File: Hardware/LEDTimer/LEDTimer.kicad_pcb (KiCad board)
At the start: 2 copper layers, 38 x 27.3 mm, 35 parts, among them J2 LED, J3 PWR_IN, SW1 SW_Push, SW2 SW_Push, SW3 SW_Push, SW4 SW_SPDT, U1 AP7383-36WW7, U2 PIC16F1825, U3 Display_128x64_096_I2C, U4 BCR_421U_E6327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

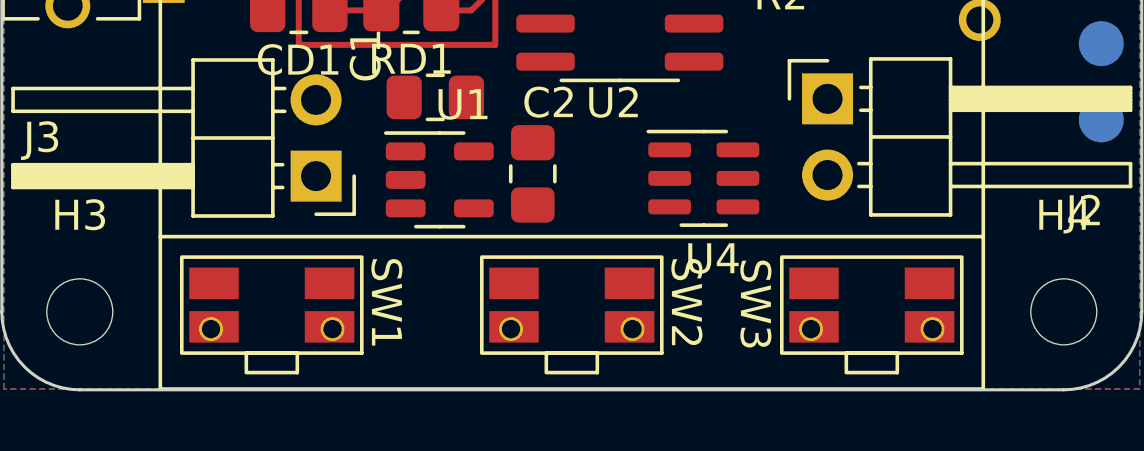
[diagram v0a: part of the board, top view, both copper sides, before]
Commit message: PCB: move the switches closer to the edge
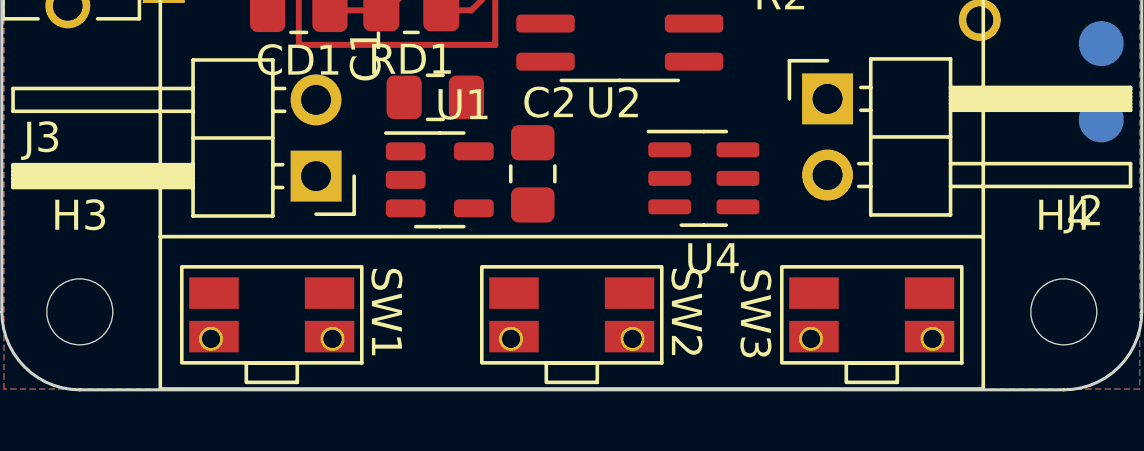
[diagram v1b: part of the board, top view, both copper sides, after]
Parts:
- moved SW1 0.33 mm to (130.3, 104.3)
- moved SW2 0.33 mm to (140.3, 104.3)
- moved SW3 0.33 mm to (150.3, 104.3)
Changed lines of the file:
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@@
   )
   (footprint "LEDTimer:EVQ9P701P" (layer "F.Cu")
-    (at 150.3 103.975 180)
+    (at 150.3 104.3 180)
     (property "Sheetfile" "LEDTimer.kicad_sch")
     (property "Sheetname" "")
@@
   )
   (footprint "LEDTimer:EVQ9P701P" (layer "F.Cu")
-    (at 140.3 103.975 180)
+    (at 140.3 104.3 180)
     (property "Sheetfile" "LEDTimer.kicad_sch")
     (property "Sheetname" "")
@@
   )
   (footprint "LEDTimer:EVQ9P701P" (layer "F.Cu")
-    (at 130.3 103.975 180)
-    (property "Sheetfile" "LEDTimer.kicad_sch")
-    (property "Sheetname" "")
+    (at 130.3 104.3 180)
+    (property "Sheetfile" "LEDTimer.kicad_sch")
+    (property "Sheetname" "")

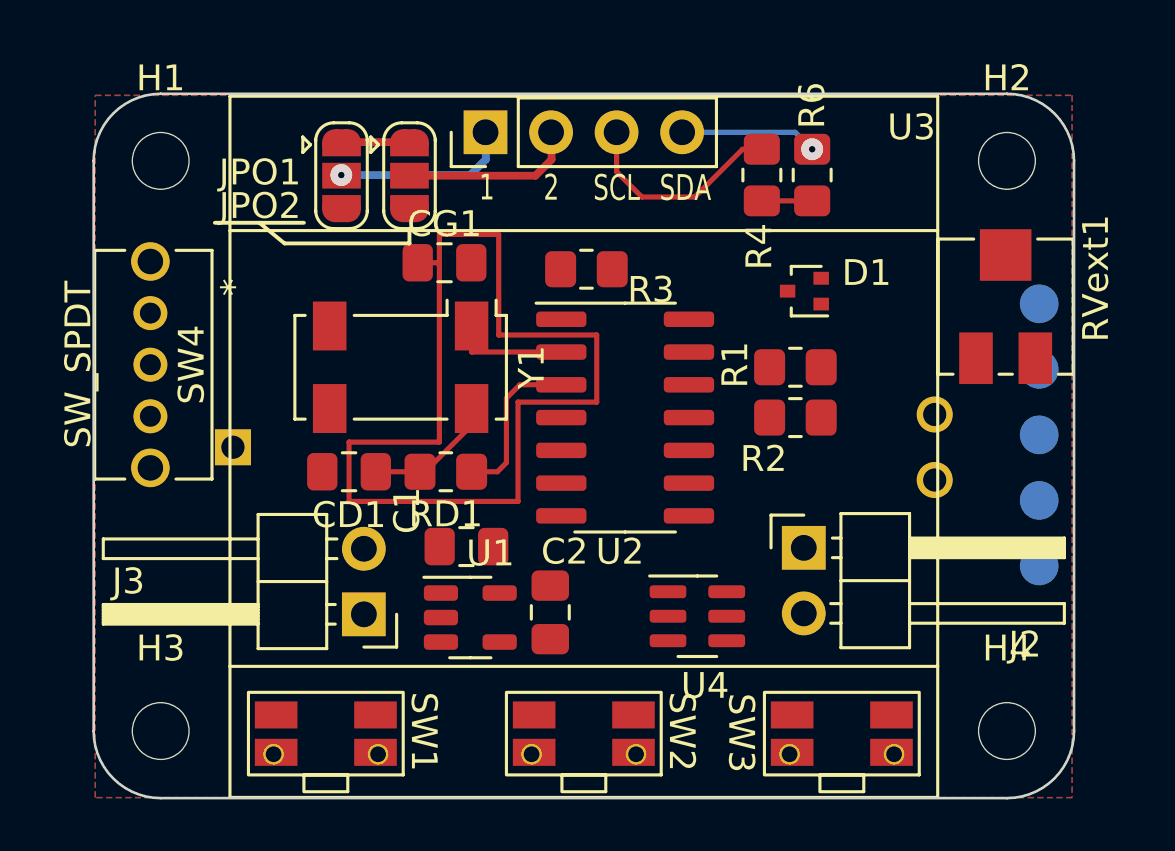
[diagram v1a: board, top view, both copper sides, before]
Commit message: PCB: use a 4-layer design
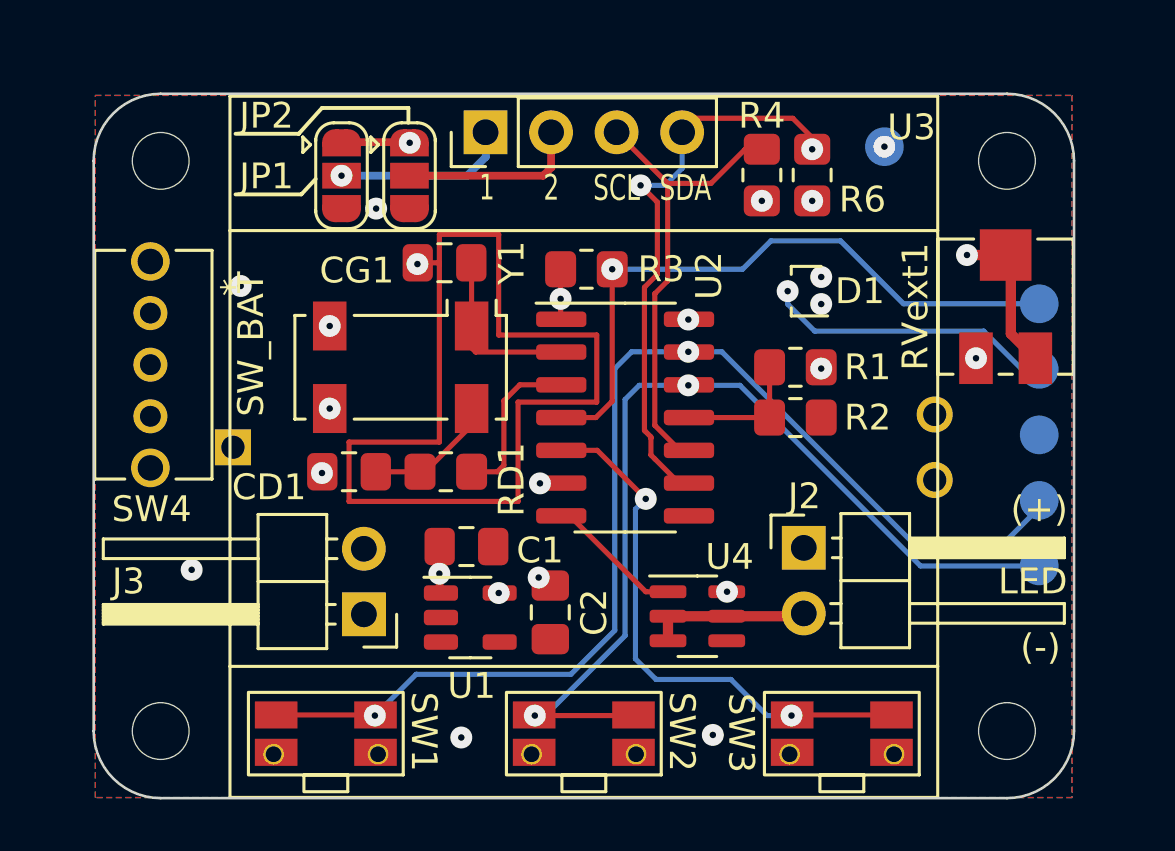
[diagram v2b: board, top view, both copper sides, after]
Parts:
- added TP6: UART_TX, TestPoint:TestPoint_Pad_D1.5mm, B.Cu at (151.9, 81.5)
- SW4: value SW_SPDT -> SW_BAT
- renumbered JPO1 to JP1, JPO2 to JP2
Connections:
- SW4 pad 1: Net-(BT1-Pad2) -> unconnected-(SW4-Pad1)
- SW4 pad 3: unconnected-(SW4-Pad3) -> Net-(BT1-Pad2)
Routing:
- net Net-(D1-Pad2): track 0.00 -> 48.6 mm, vias 0 -> 1
- net Net-(BT1-Pad2): track 0.00 -> 47.9 mm
- net /ICSPDAT: track 0.00 -> 45.7 mm, vias 0 -> 2
- net /ICSPCLK: track 0.00 -> 36.9 mm, vias 0 -> 2
- net +3V3: track 4.59 -> 40.7 mm, vias 0 -> 5
- net Net-(RVext1-Pad1): track 0.00 -> 31.0 mm, vias 0 -> 2
- net /~{MCLR}/VPP: track 0.00 -> 25.4 mm, vias 0 -> 1
- net /UART_TX: track 0.00 -> 23.3 mm, vias 0 -> 2
- net +5V: track 0.00 -> 21.5 mm, vias 0 -> 1
- net Net-(SW3-Pad2): track 0.00 -> 21.2 mm, vias 0 -> 2
- net Net-(C2-Pad1): track 0.00 -> 19.4 mm, vias 0 -> 4
- net Net-(R6-Pad2): track 5.31 -> 22.3 mm, vias 1 -> 2
- net Net-(R4-Pad2): track 8.33 -> 18.3 mm
- net Net-(J2-Pad2): track 0.00 -> 6.26 mm
- net /LED_EN_PWM: track 0.00 -> 5.36 mm
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- added copper zone on In1.Cu, net GND
- added copper zone on In2.Cu, net GND
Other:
- copper layers 2 -> 4
- board text added: "(+)"
- board text added: "(-)"

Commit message: PCB: fix DRC issues
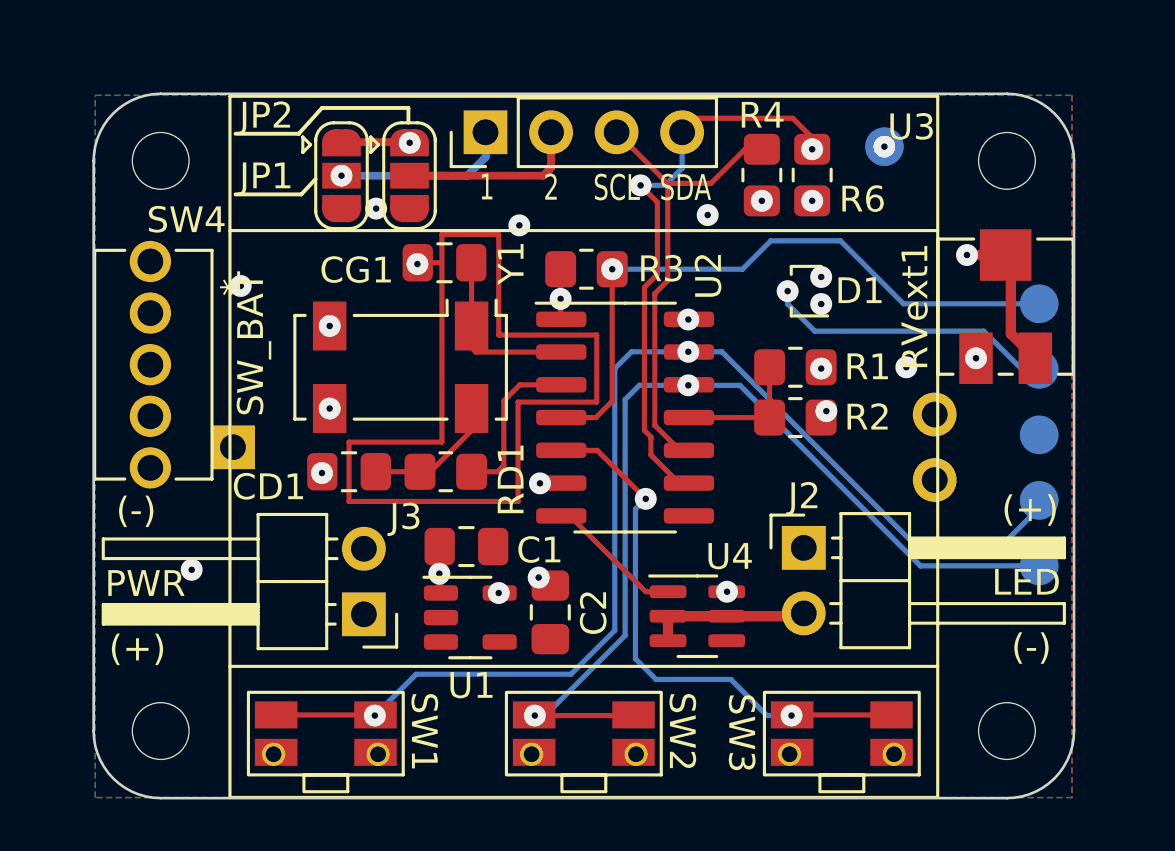
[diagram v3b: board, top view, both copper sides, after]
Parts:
- J3: value PWR_IN -> PWR
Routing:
- net GND: vias 11 -> 13
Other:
- board text added: "JLCJLCJLCJLC"
- board text added: "LED Timer V1"
- board text added: "github: tomikaa87"

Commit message: PCB: flip the power input connector
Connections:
- J3 pad 1: +5V -> GND
- J3 pad 2: GND -> +5V
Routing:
- net +5V: track 21.5 -> 22.4 mm
- net Net-(C2-Pad1): track 19.4 -> 19.7 mm, vias 4 -> 3
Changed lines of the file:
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@@
     (fp_line (start -0.32 -0.32) (end 1.5 -0.32) (layer "F.Fab") (width 0.1))
     (pad "1" thru_hole rect (at 0 0 180) (size 1.7 1.7) (drill 1) (layers *.Cu *.Mask)
-      (net 1 "+5V") (pinfunction "Pin_1") (pintype "passive"))
+      (net 2 "GND") (pinfunction "Pin_1") (pintype "passive"))
     (pad "2" thru_hole oval (at 0 2.54 180) (size 1.7 1.7) (drill 1) (layers *.Cu *.Mask)
-      (net 2 "GND") (pinfunction "Pin_2") (pintype "passive"))
+      (net 1 "+5V") (pinfunction "Pin_2") (pintype "passive"))
     (model "${KICAD6_3DMODEL_DIR}/Connector_PinHeader_2.54mm.3dshapes/PinHeader_1x02_P2.54mm_Horizontal.wrl"
       (offset (xyz 0 0 0))
@@
     (effects (font (size 1 1) (thickness 0.15)) (justify mirror))
   )
-  (gr_text "(+)" (at 123 101) (layer "F.SilkS")
+  (gr_text "(-)" (at 123 101) (layer "F.SilkS")
     (effects (font (size 1 1) (thickness 0.15)))
   )
@@
     (effects (font (size 1 1) (thickness 0.15)))
   )
-  (gr_text "(-)" (at 122.95 95.65) (layer "F.SilkS")
+  (gr_text "(+)" (at 122.95 95.65) (layer "F.SilkS")
     (effects (font (size 1 1) (thickness 0.15)))
   )
@@
   (segment (start 134.7125 97.05) (end 134.7125 98.8) (width 0.3) (layer "F.Cu") (net 1))
   (via (at 134.7 98.1) (size 0.85) (drill 0.25) (layers "F.Cu" "B.Cu") (net 1))
-  (segment (start 134.7 99.65) (end 134.725 99.675) (width 0.3) (layer "In1.Cu") (net 1))
-  (segment (start 131.775 99.675) (end 134.725 99.675) (width 0.4) (layer "In1.Cu") (net 1))
-  (segment (start 134.725 99.675) (end 138.825 99.675) (width 0.4) (layer "In1.Cu") (net 1))
-  (segment (start 141.4 97.1) (end 148.825 97.1) (width 0.4) (layer "In1.Cu") (net 1))
-  (segment (start 138.825 99.675) (end 141.4 97.1) (width 0.4) (layer "In1.Cu") (net 1))
-  (segment (start 134.7 98.1) (end 134.7 99.65) (width 0.3) (layer "In1.Cu") (net 1))
+  (segment (start 135.2 100.2) (end 134.7 99.7) (width 0.4) (layer "In1.Cu") (net 1))
+  (segment (start 148.825 97.1) (end 141.4 97.1) (width 0.4) (layer "In1.Cu") (net 1))
+  (segment (start 133.735 97.135) (end 134.7 98.1) (width 0.4) (layer "In1.Cu") (net 1))
+  (segment (start 134.7 99.7) (end 134.7 98.1) (width 0.4) (layer "In1.Cu") (net 1))
+  (segment (start 141.4 97.1) (end 138.3 100.2) (width 0.4) (layer "In1.Cu") (net 1))
+  (segment (start 138.3 100.2) (end 135.2 100.2) (width 0.4) (layer "In1.Cu") (net 1))
+  (segment (start 131.775 97.135) (end 133.735 97.135) (width 0.4) (layer "In1.Cu") (net 1))
   (via (at 132.25 83.95) (size 0.85) (drill 0.25) (layers "F.Cu" "B.Cu") (free) (net 2))
   (via (at 125.1 97.95) (size 0.85) (drill 0.25) (layers "F.Cu" "B.Cu") (free) (net 2))
@@
   (via (at 130.45 88.5) (size 0.85) (drill 0.25) (layers "F.Cu" "B.Cu") (net 2))
   (via (at 127 86.95) (size 0.85) (drill 0.25) (layers "F.Cu" "B.Cu") (free) (net 2))
+  (segment (start 137.0375 98.85) (end 138.7125 98.85) (width 0.3) (layer "F.Cu") (net 3))
+  (segment (start 138.7125 98.85) (end 139 98.5625) (width 0.3) (layer "F.Cu") (net 3))
   (via (at 149.5 87.65) (size 0.85) (drill 0.25) (layers "F.Cu" "B.Cu") (net 3))
   (via (at 149.5 90.15) (size 0.85) (drill 0.25) (layers "F.Cu" "B.Cu") (net 3))
-  (via (at 137 98.85) (size 0.85) (drill 0.25) (layers "F.Cu" "B.Cu") (net 3))
   (via (at 138.55 98.25) (size 0.85) (drill 0.25) (layers "F.Cu" "B.Cu") (net 3))
-  (segment (start 137 98.85) (end 137.95 98.85) (width 0.3) (layer "In2.Cu") (net 3))
-  (segment (start 137.95 98.85) (end 138.55 98.25) (width 0.3) (layer "In2.Cu") (net 3))
   (segment (start 149.5 90.25) (end 149.5 90.15) (width 0.3) (layer "In2.Cu") (net 3))
   (segment (start 146.7 93.05) (end 149.5 90.25) (width 0.3) (layer "In2.Cu") (net 3))
@@
   (segment (start 138.55 98.25) (end 138.55 97) (width 0.3) (layer "In2.Cu") (net 3))
   (segment (start 132.2375 94.15) (end 133.95 94.15) (width 0.2) (layer "F.Cu") (net 4))
-  (segment (start 135.95 92.55) (end 135.95 91.7) (width 0.2) (layer "F.Cu") (net 4))
-  (segment (start 133.95 94.15) (end 134.35 94.15) (width 0.2) (layer "F.Cu") (net 4))
-  (segment (start 134.35 94.15) (end 135.95 92.55) (width 0.2) (layer "F.Cu") (net 4))
+  (segment (start 133.95 94.15) (end 134.25 94.15) (width 0.2) (layer "F.Cu") (net 4))
+  (segment (start 135.95 92.45) (end 135.95 91.7) (width 0.2) (layer "F.Cu") (net 4))
+  (segment (start 134.25 94.15) (end 135.95 92.45) (width 0.2) (layer "F.Cu") (net 4))
   (segment (start 135.95 86.0625) (end 135.95 88.5) (width 0.2) (layer "F.Cu") (net 5))
   (segment (start 135.9375 86.05) (end 135.95 86.0625) (width 0.2) (layer "F.Cu") (net 5))
@@
   (segment (start 149.25 88.7) (end 148.2 87.65) (width 0.2) (layer "B.Cu") (net 7))
   (segment (start 155.8 88.7) (end 149.25 88.7) (width 0.2) (layer "B.Cu") (net 7))
-  (segment (start 140.765685 92.05) (end 141.4 91.415685) (width 0.2) (layer "F.Cu") (net 8))
-  (segment (start 139.425 92.05) (end 140.765685 92.05) (width 0.2) (layer "F.Cu") (net 8))
-  (segment (start 141.4 91.415685) (end 141.4 86.3) (width 0.2) (layer "F.Cu") (net 8))
+  (segment (start 141.057843 92.05) (end 141.4 91.707843) (width 0.2) (layer "F.Cu") (net 8))
+  (segment (start 139.425 92.05) (end 141.057843 92.05) (width 0.2) (layer "F.Cu") (net 8))
+  (segment (start 141.4 91.707843) (end 141.4 86.3) (width 0.2) (layer "F.Cu") (net 8))
   (via (at 141.4 86.3) (size 0.85) (drill 0.25) (layers "F.Cu" "B.Cu") (net 8))
   (segment (start 157.95 87.64) (end 152.69 87.64) (width 0.2) (layer "B.Cu") (net 8))
@@
   (segment (start 151.95 84.15) (end 151.95 81.55) (width 0.2) (layer "In1.Cu") (net 17))
   (segment (start 140.9 94.6) (end 138.6 94.6) (width 0.2) (layer "In1.Cu") (net 17))
-  (segment (start 142.9 93.5) (end 142.9 92.85) (width 0.2) (layer "F.Cu") (net 18))
-  (segment (start 142.65 92.55) (end 142.65 87.15) (width 0.2) (layer "F.Cu") (net 18))
-  (segment (start 142.7 92.6) (end 142.65 92.55) (width 0.2) (layer "F.Cu") (net 18))
-  (segment (start 142.65 87.15) (end 142.65 87) (width 0.2) (layer "F.Cu") (net 18))
+  (segment (start 143.15 86.55) (end 143.15 83.7) (width 0.2) (layer "F.Cu") (net 18))
   (segment (start 144.652 80.45) (end 144.11 80.992) (width 0.2) (layer "F.Cu") (net 18))
-  (segment (start 143.05 93.65) (end 142.9 93.5) (width 0.2) (layer "F.Cu") (net 18))
-  (segment (start 143.15 86.5) (end 143.15 86.05) (width 0.2) (layer "F.Cu") (net 18))
+  (segment (start 144.375 94.59) (end 143.99 94.59) (width 0.2) (layer "F.Cu") (net 18))
   (segment (start 148.4 80.45) (end 144.652 80.45) (width 0.2) (layer "F.Cu") (net 18))
-  (segment (start 142.9 92.85) (end 142.9 92.8) (width 0.2) (layer "F.Cu") (net 18))
-  (segment (start 143.1 86.55) (end 143.15 86.5) (width 0.2) (layer "F.Cu") (net 18))
-  (segment (start 142.9 92.8) (end 142.7 92.6) (width 0.2) (layer "F.Cu") (net 18))
-  (segment (start 143.99 94.59) (end 143.05 93.65) (width 0.2) (layer "F.Cu") (net 18))
+  (segment (start 142.65 93.25) (end 142.65 87.05) (width 0.2) (layer "F.Cu") (net 18))
+  (segment (start 143.15 83.7) (end 142.5 83.05) (width 0.2) (layer "F.Cu") (net 18))
   (segment (start 149.15 81.2) (end 148.4 80.45) (width 0.2) (layer "F.Cu") (net 18))
-  (segment (start 144.375 94.59) (end 143.99 94.59) (width 0.2) (layer "F.Cu") (net 18))
+  (segment (start 142.65 87.05) (end 143.15 86.55) (width 0.2) (layer "F.Cu") (net 18))
   (segment (start 149.15 81.65) (end 149.15 81.2) (width 0.2) (layer "F.Cu") (net 18))
-  (segment (start 143.15 86.05) (end 143.15 83.7) (width 0.2) (layer "F.Cu") (net 18))
-  (segment (start 143.15 83.7) (end 142.5 83.05) (width 0.2) (layer "F.Cu") (net 18))
-  (segment (start 142.65 87) (end 143.1 86.55) (width 0.2) (layer "F.Cu") (net 18))
+  (segment (start 143.99 94.59) (end 142.65 93.25) (width 0.2) (layer "F.Cu") (net 18))
   (via (at 142.5 83.05) (size 0.85) (drill 0.25) (layers "F.Cu" "B.Cu") (net 18))
   (via (at 149.15 81.65) (size 0.85) (drill 0.25) (layers "F.Cu" "B.Cu") (net 18))
